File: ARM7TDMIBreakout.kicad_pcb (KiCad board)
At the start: 2 copper layers, 64.5 x 28.7 mm, 8 parts, among them J1 Conn_01x24_MountingPin_24-1, J2 Conn_01x24_MountingPin_48-1, U1 ARM7TDMI

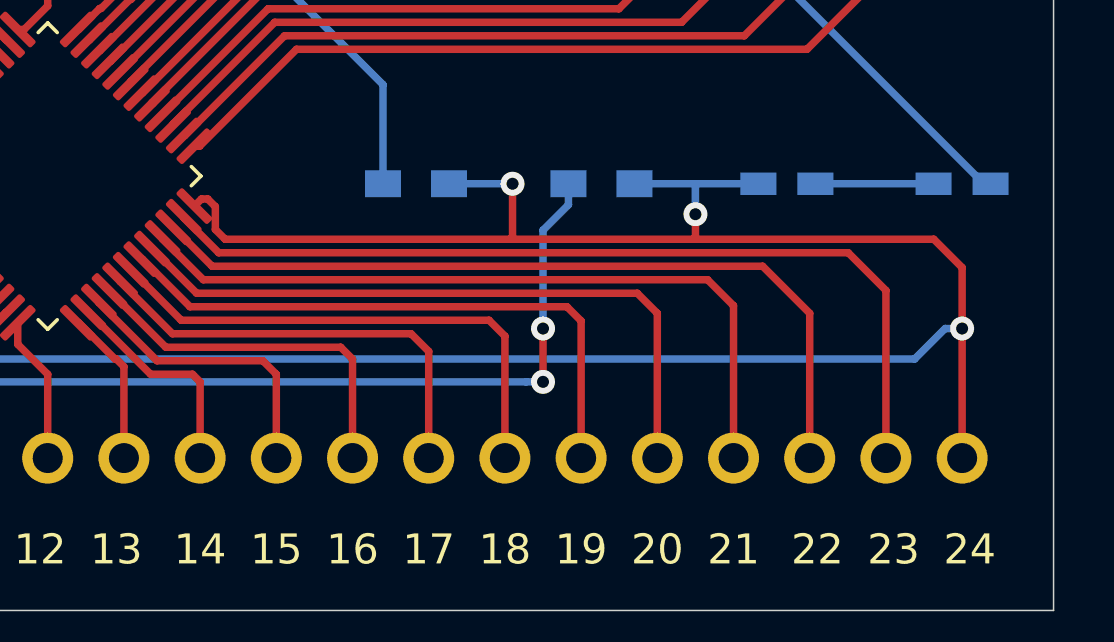
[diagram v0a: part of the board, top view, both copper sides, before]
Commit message: Fixed: Connected bypass capacitors to AGND
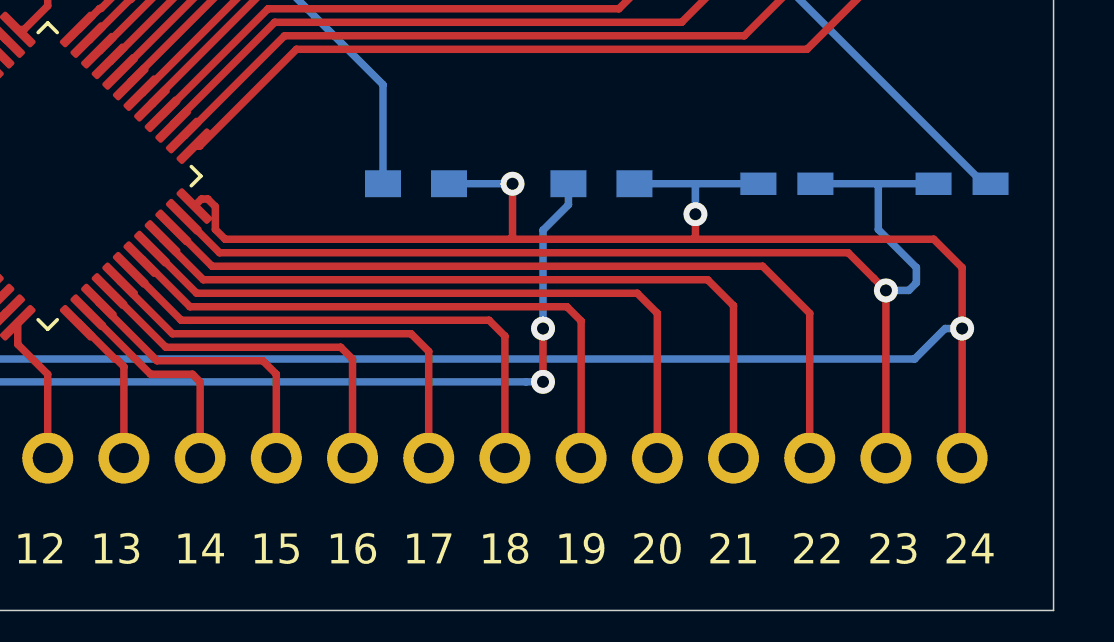
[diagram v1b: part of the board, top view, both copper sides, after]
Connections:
- J1 pad 23: Net-(J1-Pad23) -> GND
- U1 pad 23: Net-(J1-Pad23) -> GND
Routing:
- net GND: track 3.94 -> 38.9 mm, vias 0 -> 1
- net Net-(J1-Pad23): track 29.8 -> 0.00 mm
